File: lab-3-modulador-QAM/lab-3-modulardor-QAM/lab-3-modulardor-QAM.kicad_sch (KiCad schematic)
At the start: 57 parts, among them Q2 2N3904, U1 LM741, U2 LM741, U3 LM741, U4 MC1496, U5 MC1496, U6 LM741

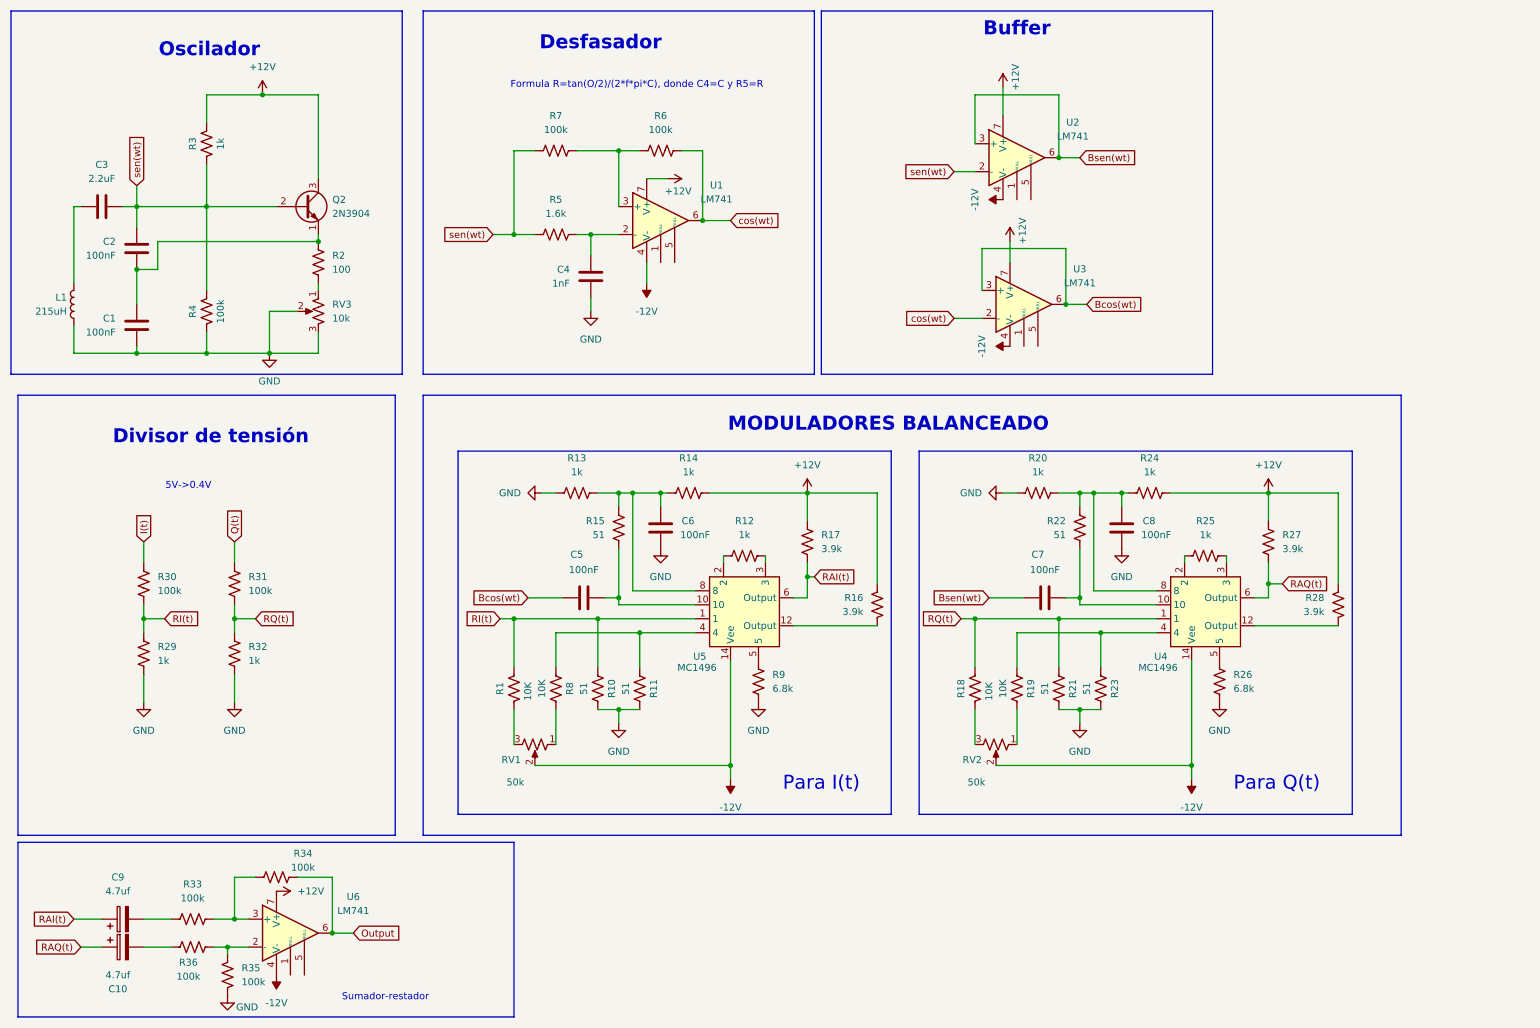
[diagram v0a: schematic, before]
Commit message: Cambiando los buffer por lm358 e iniciando enrutado
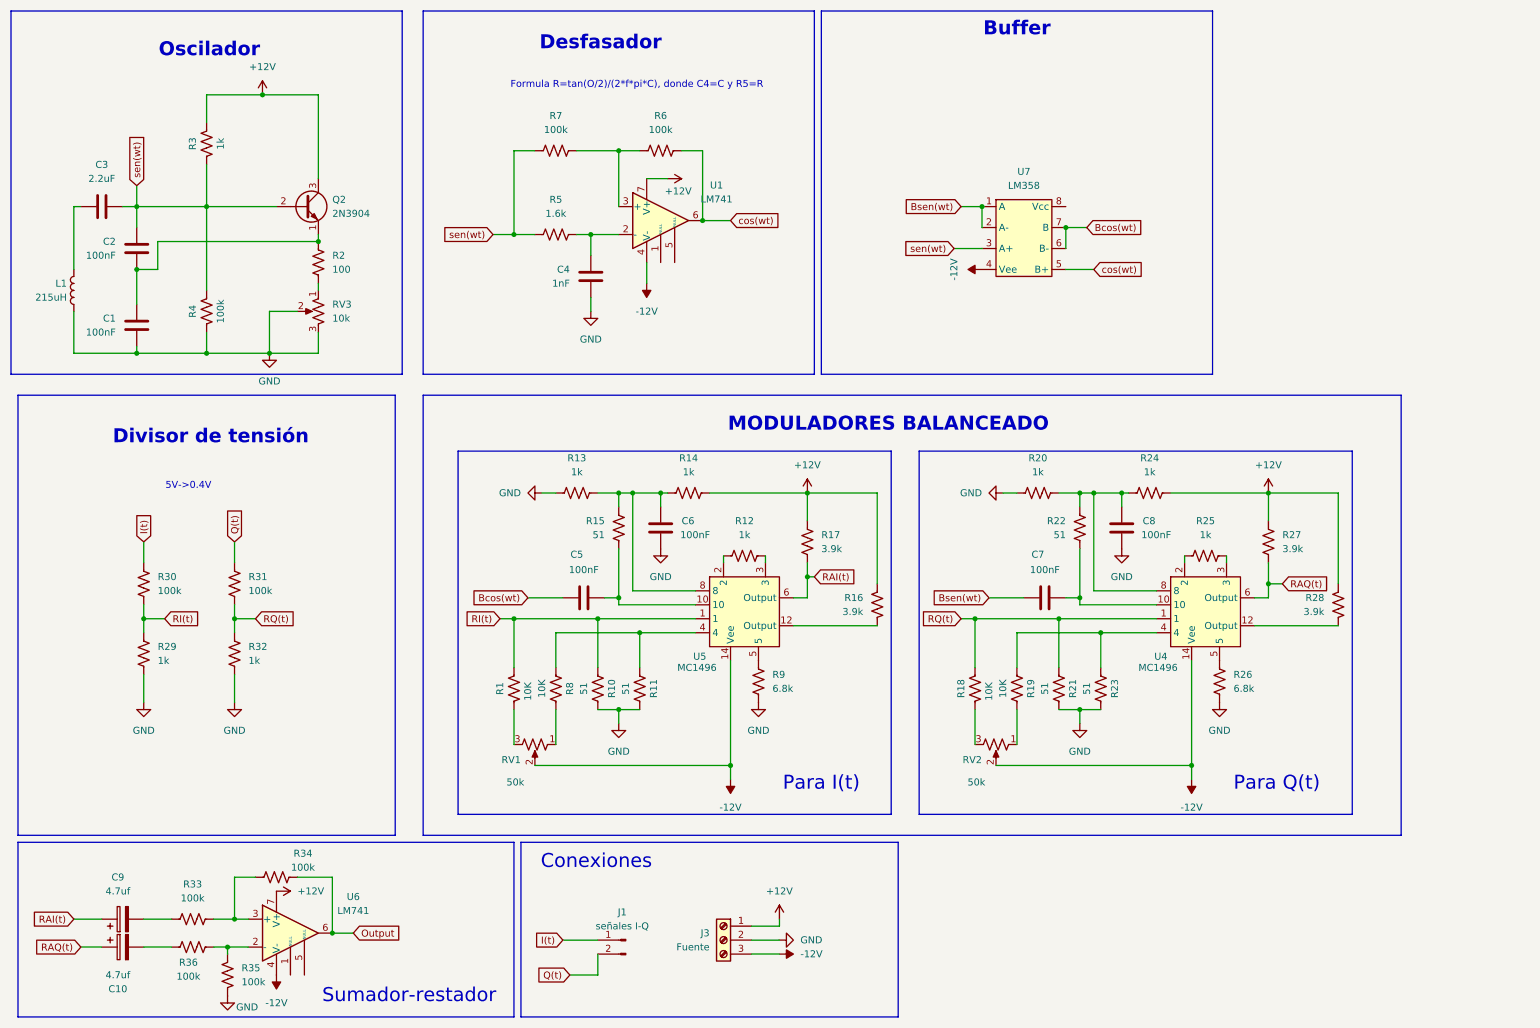
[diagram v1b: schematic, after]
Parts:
- removed U2, U3: LM741, symbol Amplifier_Operational:LM741
- added J1: señales I-Q, Connector_PinHeader_1.00mm:PinHeader_1x02_P1.00mm_Horizontal, symbol Connector:Conn_01x02_Pin
- added J3: Fuente, TerminalBlock_RND:TerminalBlock_RND_205-00002_1x03_P5.00mm_Horizontal, symbol Connector:Screw_Terminal_01x03
- added U7: LM358, Package_DIP:DIP-8_W10.16mm, symbol otros_componentes:LM358
- C1, C2, C4, C5, C6, C7, C8: footprint (none) -> Capacitor_THT:C_Disc_D3.0mm_W1.6mm_P2.50mm
- C10, C9: footprint (none) -> Capacitor_THT:CP_Radial_D4.0mm_P1.50mm
- C3: footprint (none) -> Capacitor_THT:C_Disc_D4.3mm_W1.9mm_P5.00mm
- L1: footprint (none) -> Inductor_THT:L_Axial_L5.3mm_D2.2mm_P2.54mm_Vertical_Vishay_IM-1
- R1, R10, R11, R12, R13, R14, R15, R16, R17, R18, R19, R2, R20, R21, R22, R23, R24, R25, R26, R27, R28, R29, R3, R30, R31, R32, R33, R34, R35, R36, R4, R5, R6, R7, R8, R9: footprint (none) -> Resistor_THT:R_Axial_DIN0309_L9.0mm_D3.2mm_P12.70mm_Horizontal
- RV1, RV2, RV3: footprint (none) -> Potentiometer_THT:Potentiometer_Vishay_T93YA_Vertical
- U1, U6: footprint (none) -> Package_DIP:DIP-8_W7.62mm
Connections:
- net +12V: now also J3.1 (Pin_1)
- net -12V: now also J3.3 (Pin_3), U7.4 (Vee)
- net Bcos(wt): now also U7.6 (B-), U7.7 (B)
- net Bsen(wt): now also U7.1 (A), U7.2 (A-)
- net GND: now also J3.2 (Pin_2)
- net I(t): now also J1.1 (Pin_1)
- net Q(t): now also J1.2 (Pin_2)
- net cos(wt): now also U7.5 (B+)
- net sen(wt): now also U7.3 (A+)
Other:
- note added: "Conexiones"
- moved on the sheet: L1

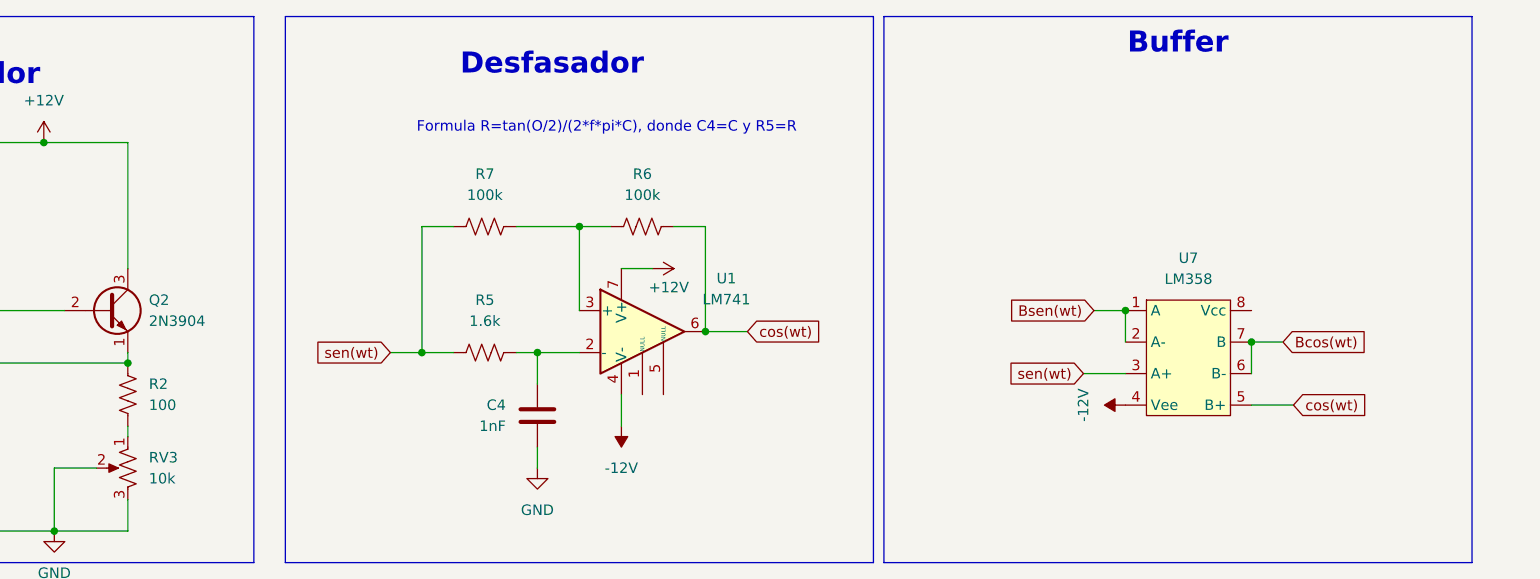
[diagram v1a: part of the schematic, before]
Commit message: Cambios en el esquematico, enrutado en pcb y correción de algunos errores
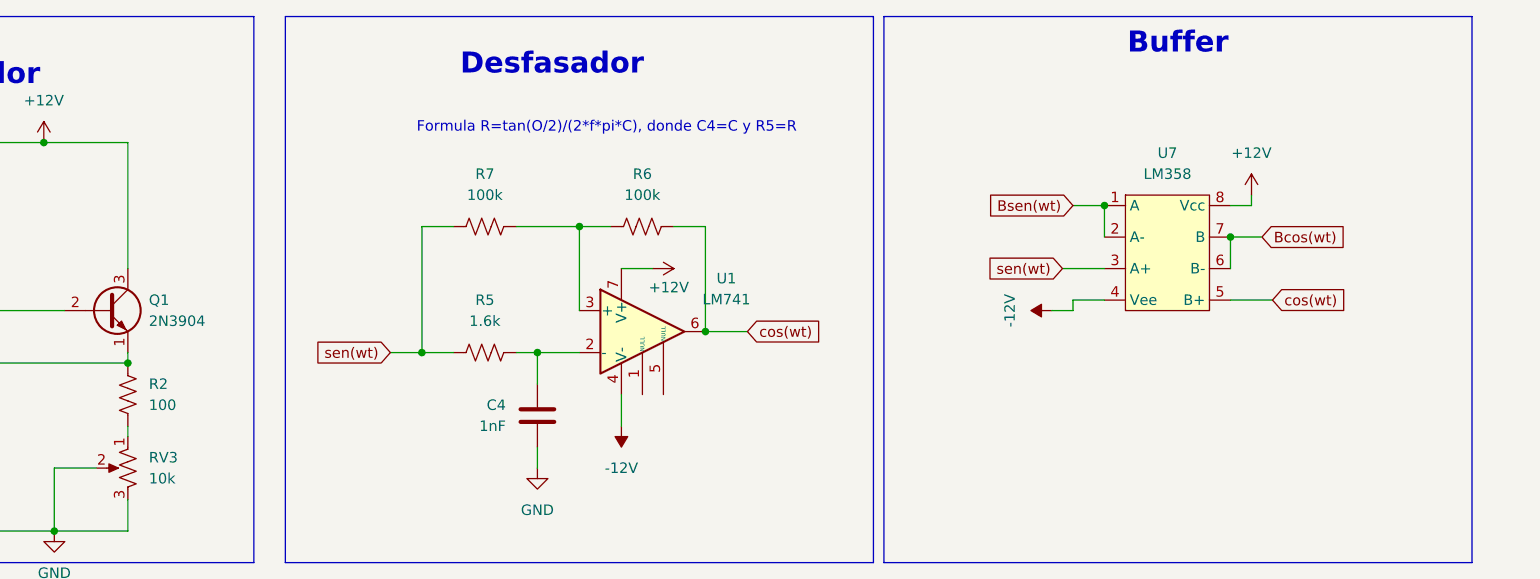
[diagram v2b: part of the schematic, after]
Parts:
- J1: footprint Connector_PinHeader_1.00mm:PinHeader_1x02_P1.00mm_Horizontal -> Connector_PinHeader_1.00mm:PinHeader_1x02_P1.00mm_Vertical
- renumbered Q2 to Q1
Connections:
- net +12V: now also U7.8 (Vcc)
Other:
- moved on the sheet: U7
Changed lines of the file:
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@@
 		(comment 1 "Luis Angel Camargo Guzman - 20221005086")
 		(comment 2 "Joan Sebastian Ramos Cuervo - 20221005091")
-		(comment 3 "Cristian Francisco Enciso")
+		(comment 3 "Cristian Camilo Franco Enciso - 20201005172")
 	)
 	(rectangle
@@
 	)
 	(junction
-		(at 204.47 54.61)
+		(at 201.93 41.91)
 		(diameter 0)
 		(color 0 0 0 0)
@@
 	)
 	(junction
-		(at 189.23 50.8)
+		(at 186.69 38.1)
 		(diameter 0)
 		(color 0 0 0 0)
@@
 	(wire
 		(pts
+			(xy 180.34 50.8) (xy 182.88 50.8)
+		)
+		(stroke
+			(width 0)
+			(type default)
+		)
+	)
+	(wire
+		(pts
 			(xy 36.83 123.19) (xy 36.83 125.73)
 		)
@@
 	(wire
 		(pts
+			(xy 182.88 50.8) (xy 182.88 49.53)
+		)
+		(stroke
+			(width 0)
+			(type default)
+		)
+	)
+	(wire
+		(pts
 			(xy 100.33 55.88) (xy 104.14 55.88)
 		)
@@
 	(wire
 		(pts
-			(xy 185.42 50.8) (xy 189.23 50.8)
+			(xy 182.88 38.1) (xy 186.69 38.1)
 		)
 		(stroke
@@
 	(wire
 		(pts
-			(xy 189.23 50.8) (xy 189.23 54.61)
+			(xy 186.69 38.1) (xy 186.69 41.91)
 		)
 		(stroke
@@
 	(wire
 		(pts
-			(xy 204.47 54.61) (xy 208.28 54.61)
+			(xy 201.93 41.91) (xy 205.74 41.91)
 		)
 		(stroke
@@
 	(wire
 		(pts
-			(xy 204.47 62.23) (xy 209.55 62.23)
+			(xy 201.93 49.53) (xy 207.01 49.53)
 		)
 		(stroke
@@
 	(wire
 		(pts
-			(xy 204.47 54.61) (xy 204.47 58.42)
+			(xy 201.93 41.91) (xy 201.93 45.72)
 		)
 		(stroke
@@
 	(wire
 		(pts
-			(xy 184.15 58.42) (xy 189.23 58.42)
+			(xy 181.61 45.72) (xy 186.69 45.72)
 		)
 		(stroke
@@
 	(wire
 		(pts
+			(xy 204.47 38.1) (xy 201.93 38.1)
+		)
+		(stroke
+			(width 0)
+			(type default)
+		)
+	)
+	(wire
+		(pts
 			(xy 49.53 185.42) (xy 52.07 185.42)
 		)
@@
 	(wire
 		(pts
+			(xy 204.47 36.83) (xy 204.47 38.1)
+		)
+		(stroke
+			(width 0)
+			(type default)
+		)
+	)
+	(wire
+		(pts
+			(xy 182.88 49.53) (xy 186.69 49.53)
+		)
+		(stroke
+			(width 0)
+			(type default)
+		)
+	)
+	(wire
+		(pts
 			(xy 123.19 102.87) (xy 123.19 105.41)
 		)
@@
 	(global_label "sen(wt)"
 		(shape input)
-		(at 184.15 58.42 180)
+		(at 181.61 45.72 180)
 		(fields_autoplaced yes)
 		(effects
@@
 		)
 		(property "Intersheetrefs" "${INTERSHEET_REFS}"
-			(at 174.1495 58.42 0)
+			(at 171.6095 45.72 0)
 			(effects
 				(font
@@
 	(global_label "Bcos(wt)"
 		(shape input)
-		(at 208.28 54.61 0)
+		(at 205.74 41.91 0)
 		(fields_autoplaced yes)
 		(effects
@@
 		)
 		(property "Intersheetrefs" "${INTERSHEET_REFS}"
-			(at 219.5505 54.61 0)
+			(at 217.0105 41.91 0)
 			(effects
 				(font
@@
 	(global_label "Bsen(wt)"
 		(shape input)
-		(at 185.42 50.8 180)
+		(at 182.88 38.1 180)
 		(fields_autoplaced yes)
 		(effects
@@
 		)
 		(property "Intersheetrefs" "${INTERSHEET_REFS}"
-			(at 174.1495 50.8 0)
+			(at 171.6095 38.1 0)
 			(effects
 				(font
@@
 	(global_label "cos(wt)"
 		(shape input)
-		(at 209.55 62.23 0)
+		(at 207.01 49.53 0)
 		(fields_autoplaced yes)
 		(effects
@@
 		)
 		(property "Intersheetrefs" "${INTERSHEET_REFS}"
-			(at 219.5505 62.23 0)
+			(at 217.0105 49.53 0)
 			(effects
 				(font
@@
 	(symbol
 		(lib_id "power:-12V")
-		(at 189.23 62.23 90)
+		(at 180.34 50.8 90)
 		(mirror x)
 		(unit 1)
@@
 		(dnp no)
 		(property "Reference" "#PWR8"
-			(at 193.04 62.23 0)
+			(at 184.15 50.8 0)
 			(effects
 				(font
@@
 		)
 		(property "Value" "-12V"
-			(at 184.15 62.23 0)
+			(at 175.26 50.8 0)
 			(effects
 				(font
@@
 		)
 		(property "Footprint" ""
-			(at 189.23 62.23 0)
+			(at 180.34 50.8 0)
 			(effects
 				(font
@@
 		)
 		(property "Datasheet" ""
-			(at 189.23 62.23 0)
+			(at 180.34 50.8 0)
 			(effects
 				(font
@@
 		)
 		(property "Description" "Power symbol creates a global label with name \"-12V\""
-			(at 189.23 62.23 0)
+			(at 180.34 50.8 0)
 			(effects
 				(font
@@
 	)
 	(symbol
+		(lib_id "power:+12V")
+		(at 204.47 36.83 0)
+		(unit 1)
+		(exclude_from_sim no)
+		(in_bom yes)
+		(on_board yes)
+		(dnp no)
+		(fields_autoplaced yes)
+		(property "Reference" "#PWR06"
+			(at 204.47 40.64 0)
+			(effects
+				(font
+					(size 1.27 1.27)
+				)
+				(hide yes)
+			)
+		)
+		(property "Value" "+12V"
+			(at 204.47 31.75 0)
+			(effects
+				(font
+					(size 1.27 1.27)
+				)
+			)
+		)
+		(property "Footprint" ""
+			(at 204.47 36.83 0)
+			(effects
+				(font
+					(size 1.27 1.27)
+				)
+				(hide yes)
+			)
+		)
+		(property "Datasheet" ""
+			(at 204.47 36.83 0)
+			(effects
+				(font
+					(size 1.27 1.27)
+				)
+				(hide yes)
+			)
+		)
+		(property "Description" "Power symbol creates a global label with name \"+12V\""
+			(at 204.47 36.83 0)
+			(effects
+				(font
+					(size 1.27 1.27)
+				)
+				(hide yes)
+			)
+		)
+		(pin "1"
+		)
+		(instances
+			(project ""
+				(path "/be553ecb-da65-43ec-9fc5-3aeb6eae0634"
+					(reference "#PWR06")
+					(unit 1)
+				)
+			)
+		)
+	)
+	(symbol
 		(lib_id "Device:R_Potentiometer_US")
 		(at 107.95 148.59 270)
@@
 	(symbol
 		(lib_id "otros_componentes:LM358")
-		(at 196.85 44.45 0)
+		(at 194.31 31.75 0)
 		(unit 1)
 		(exclude_from_sim no)
@@
 		(fields_autoplaced yes)
 		(property "Reference" "U7"
-			(at 196.85 44.45 0)
+			(at 194.31 31.75 0)
 			(effects
 				(font
@@
 		)
 		(property "Value" "LM358"
-			(at 196.85 46.99 0)
+			(at 194.31 34.29 0)
 			(effects
 				(font
@@
 		)
 		(property "Footprint" "Package_DIP:DIP-8_W10.16mm"
-			(at 196.088 39.37 0)
+			(at 193.548 26.67 0)
 			(effects
 				(font
@@
 		)
 		(property "Datasheet" "https://www.alldatasheet.com/datasheet-pdf/view/514875/ONSEMI/LM358.html"
-			(at 196.342 41.91 0)
+			(at 193.802 29.21 0)
 			(effects
 				(font
@@
 		)
 		(property "Description" ""
-			(at 196.85 44.45 0)
+			(at 194.31 31.75 0)
 			(effects
 				(font
@@
 			)
 		)
-		(property "Footprint" "Connector_PinHeader_1.00mm:PinHeader_1x02_P1.00mm_Horizontal"
+		(property "Footprint" "Connector_PinHeader_1.00mm:PinHeader_1x02_P1.00mm_Vertical"
 			(at 124.46 184.15 0)
 			(effects
@@
 		(dnp no)
 		(fields_autoplaced yes)
-		(property "Reference" "Q2"
+		(property "Reference" "Q1"
 			(at 71.12 49.5299 0)
 			(effects
@@
 			(project ""
 				(path "/be553ecb-da65-43ec-9fc5-3aeb6eae0634"
-					(reference "Q2")
+					(reference "Q1")
 					(unit 1)
 				)
